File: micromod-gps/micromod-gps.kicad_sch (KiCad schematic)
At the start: 62 parts, among them J1 21992304, J2 Conn_01x08_Socket, Q1 2N7002, Q2 DMP510DL-7, SW1 KMR2, SW2 KMR2, U1 STM32G431CBTx, U10 TLV75533PDBV, U4 LMR51430, Y1 ECS-250-10-47Q-CES-TR

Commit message: tweaks
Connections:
- net MCU_UART_TX2: now reaches U1.10 (PA2)
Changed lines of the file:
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@@
-	)
-	(no_connect
-		(at 207.645 63.5)
 	)
 	(no_connect
@@
 	)
 	(no_connect
+		(at 229.235 63.5)
+	)
+	(no_connect
 		(at 318.135 65.405)
 	)
@@
 	(wire
 		(pts
+			(xy 207.645 63.5) (xy 229.235 63.5)
+		)
+		(stroke
+			(width 0)
+			(type default)
+		)
+	)
+	(wire
+		(pts
 			(xy 243.84 126.365) (xy 254.635 126.365)
 		)
@@
 		)
 	)
+	(label "MCU_UART_TX2"
+		(at 213.36 63.5 0)
+		(effects
+			(font
+				(size 1.27 1.27)
+			)
+			(justify left bottom)
+		)
+	)

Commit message: Added temp sensor and tvs diode for rs232
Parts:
- added C60: 0.1uF, Capacitor_SMD:C_0603_1608Metric_Pad1.08x0.95mm_HandSolder, symbol Device:C
- added U21: MCP9800Ax-xOT, Package_TO_SOT_SMD:SOT-23-5, symbol Sensor_Temperature:MCP9800Ax-xOT
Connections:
- net +3V3: now also C60.1, U21.1 (V_{DD})
- net GND: now also C60.2, U21.2 (GND)
- net GPS_SCL: now also U21.4 (SCLK)
- net GPS_SDA: now also U21.5 (SDA)
- net TOO_HOT: now reaches U1.28 (PB14)
- net TOO_HOT: now also U21.3 (ALERT)
- no-connect marks 48 -> 47

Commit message: Added testpoints
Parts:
- added TP10, TP11, TP2, TP3, TP4, TP5, TP8, TP9: TestPoint, SUFST:Keystone 5015, symbol Connector:TestPoint
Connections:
- net +3V3: now also TP10.1
- net +5V: now also TP9.1
- net +GLV_PROT: now also TP8.1
- net GPS_PPS: now also TP11.1
- net GPS_SCL: now also TP5.1
- net GPS_SDA: now also TP4.1
- net OFFBOARD_UART_IN: now also TP3.1
- net OFFBOARD_UART_OUT: now also TP2.1

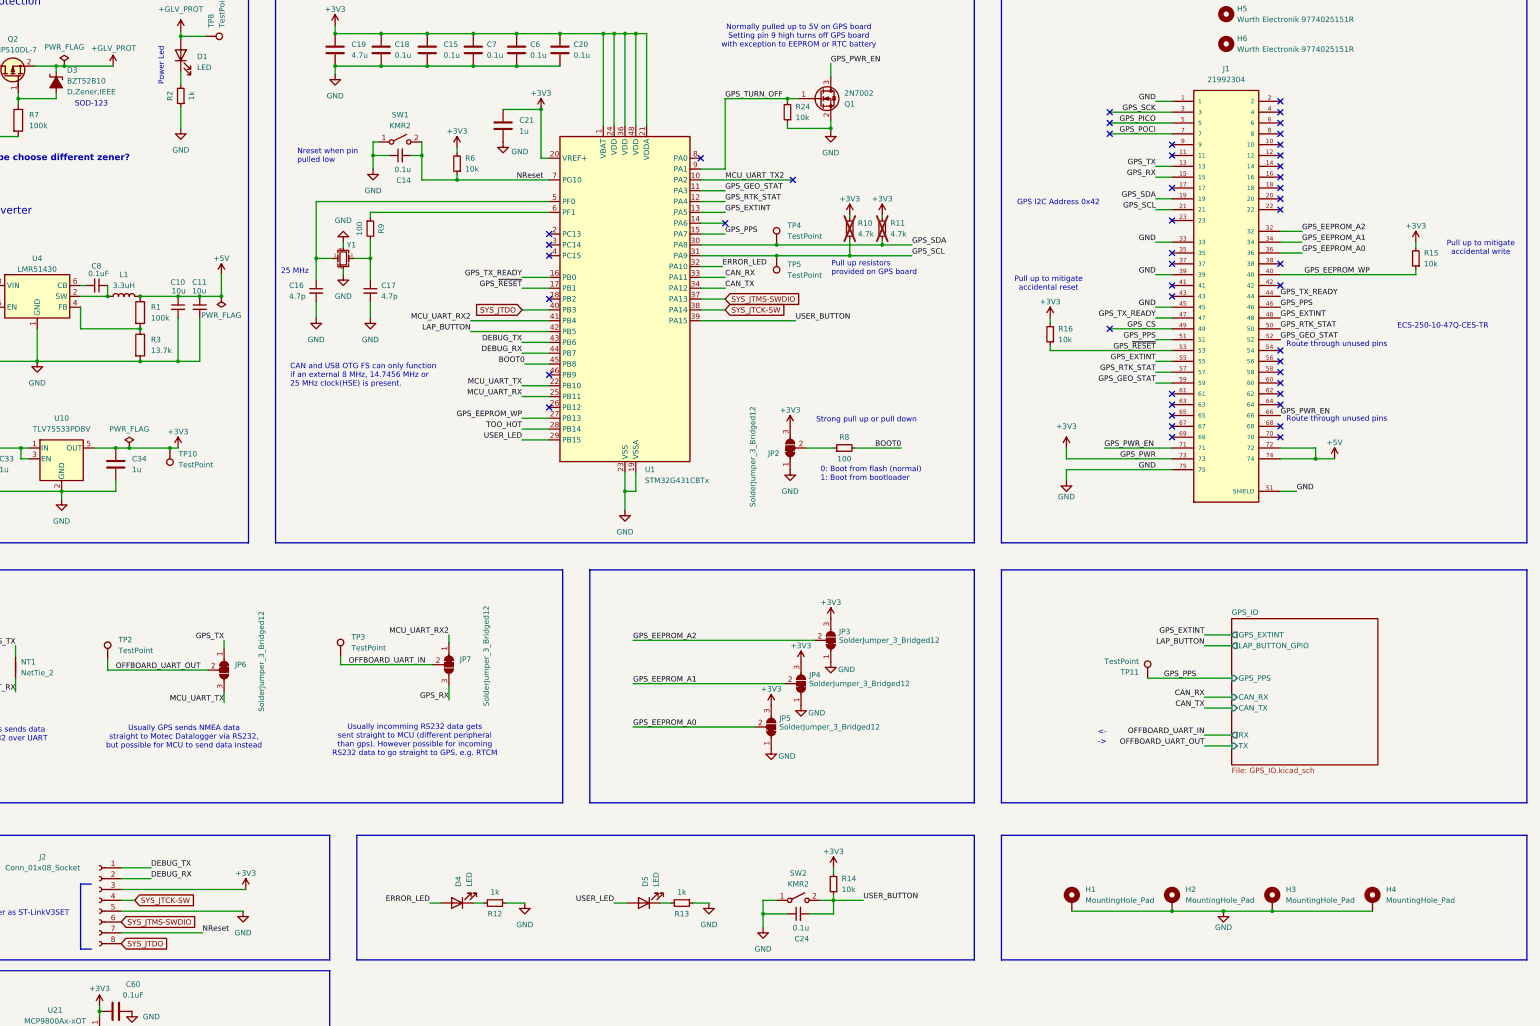
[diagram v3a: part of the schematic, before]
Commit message: rerouted some things and added SPI
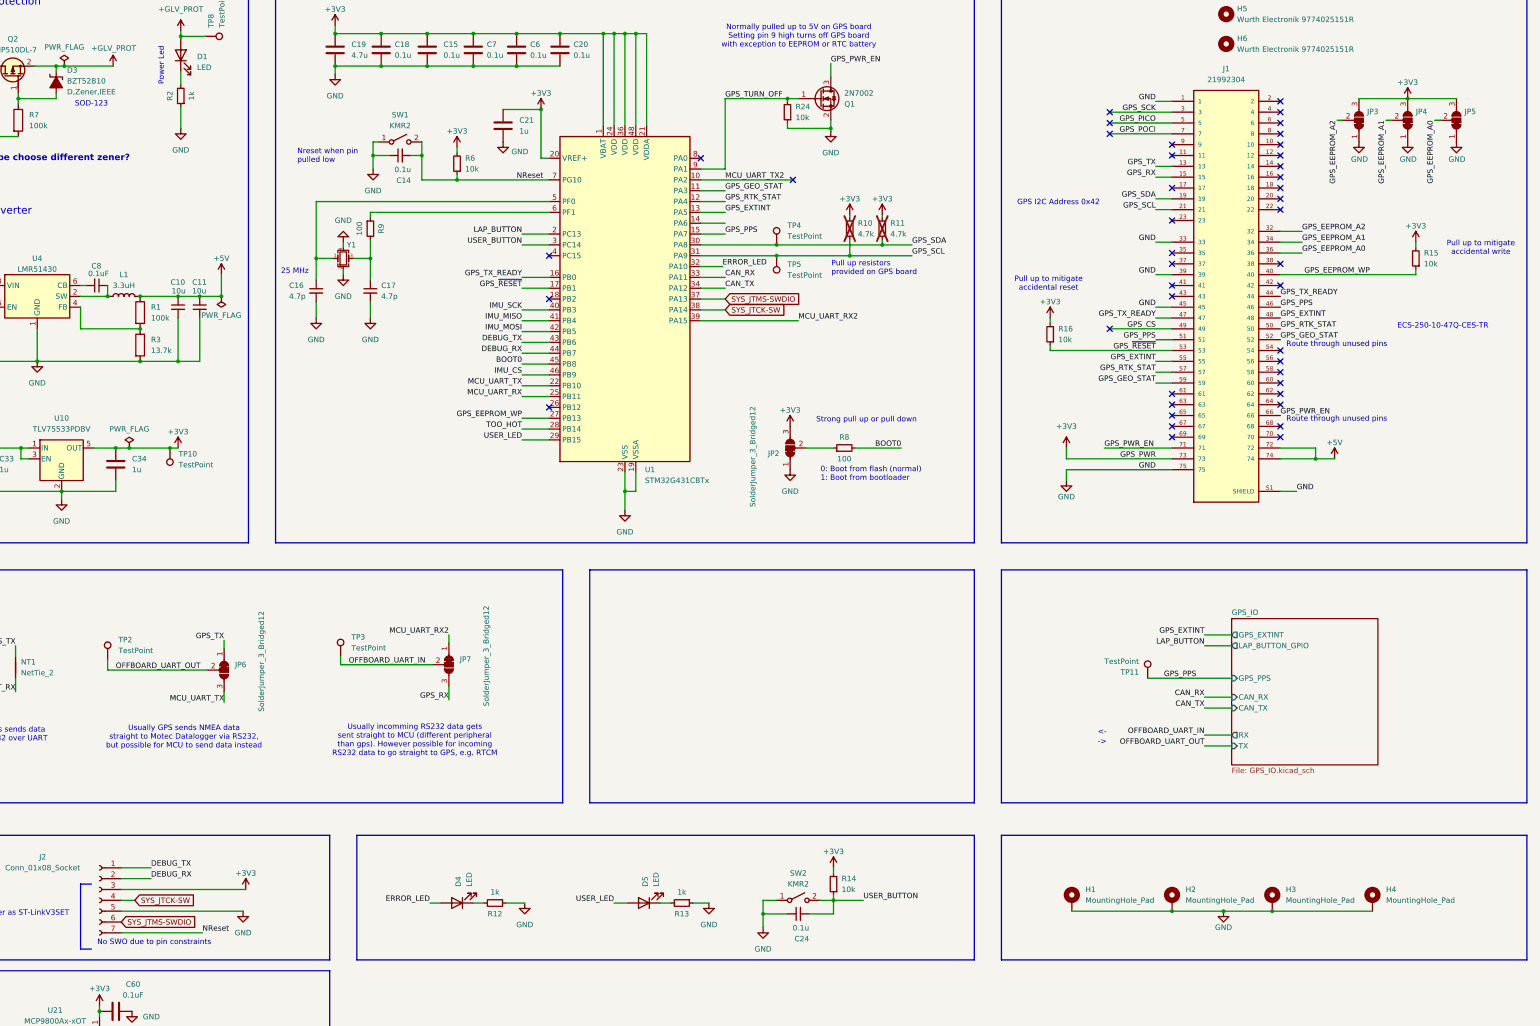
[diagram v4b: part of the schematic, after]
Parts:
- J2: footprint Connector_PinSocket_2.54mm:PinSocket_1x08_P2.54mm_Vertical -> Connector_PinSocket_2.54mm:PinSocket_1x07_P2.54mm_Vertical; symbol Connector:Conn_01x08_Socket -> Connector:Conn_01x07_Socket
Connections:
- net LAP_BUTTON: now also U1.2 (PC13); no longer U1.42 (PB5)
- net MCU_UART_RX2: now also U1.39 (PA15); no longer U1.41 (PB4)
- net USER_BUTTON: now also U1.3 (PC14); no longer U1.39 (PA15)
- net IMU_CS: now reaches U1.46 (PB9)
- net SYS_JTDO renamed IMU_SCK
- net IMU_SCK: no longer J2.8 (Pin_8)
- new net IMU_MISO: U1.41 (PB4)
- new net IMU_MOSI: U1.42 (PB5)
- no-connect marks 47 -> 43
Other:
- note added: "No SWO due to pin constraints"
- note removed: "CAN and USB OTG FS can only function if an external 8 MHz, 14.7456 MHz or 25 MHz clock(HSE) is present."
- moved on the sheet: JP3, JP4, JP5

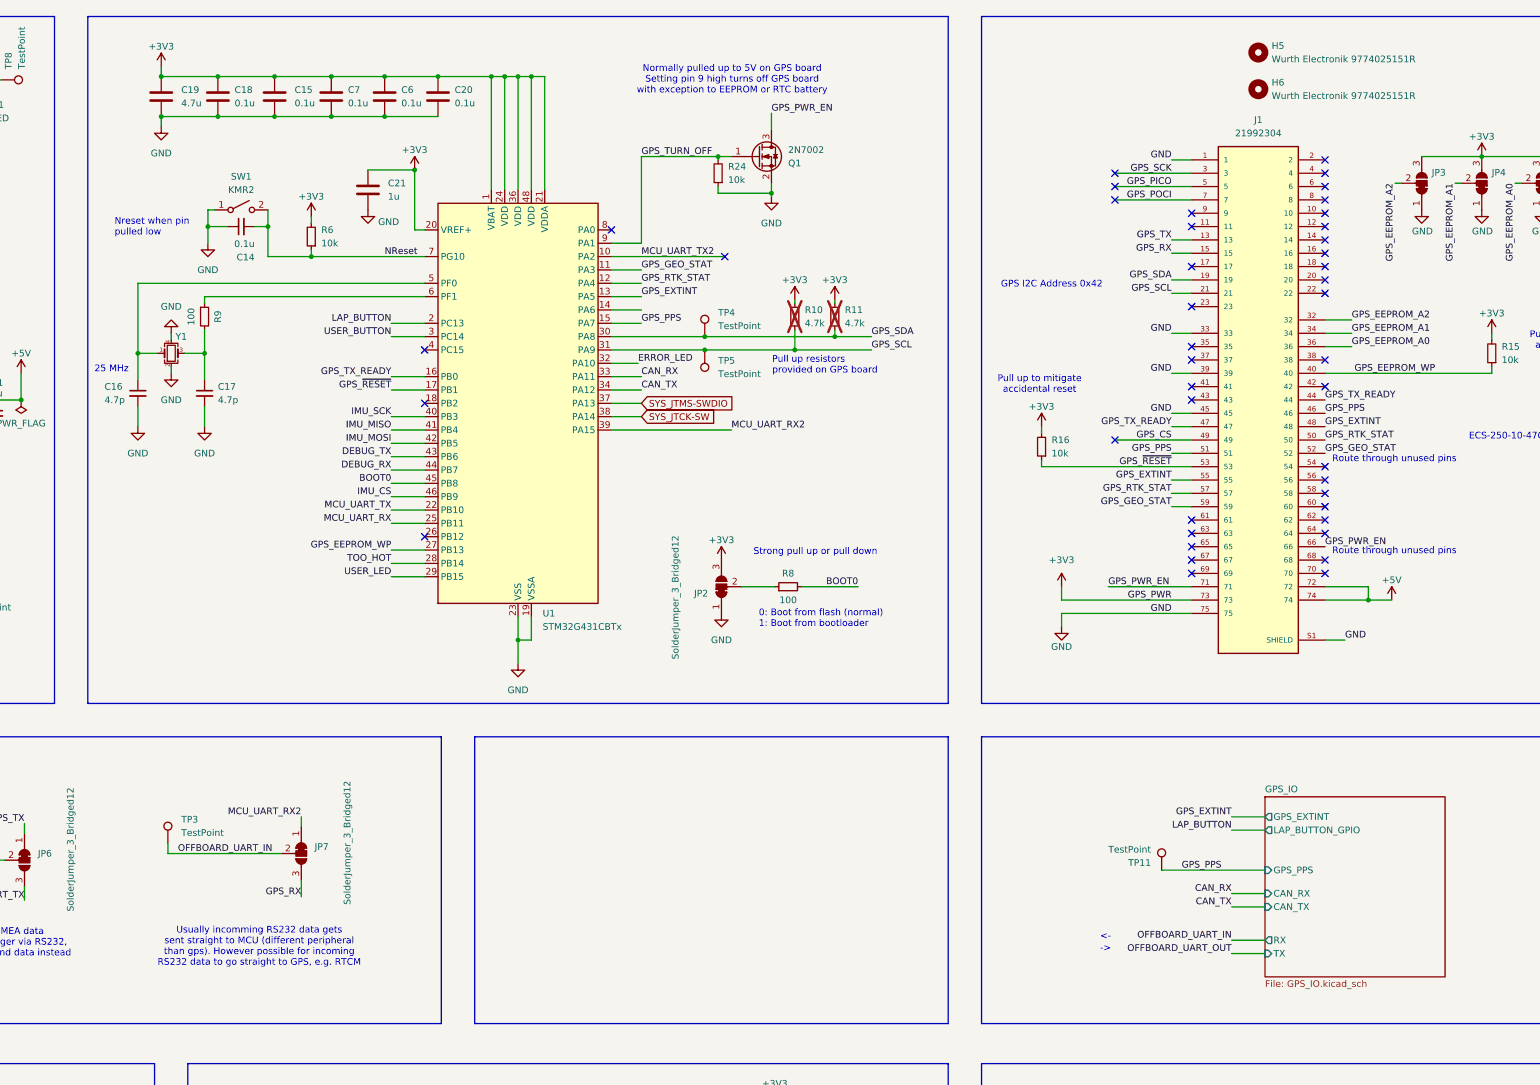
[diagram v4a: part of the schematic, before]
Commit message: Added IMU and Magnetometer
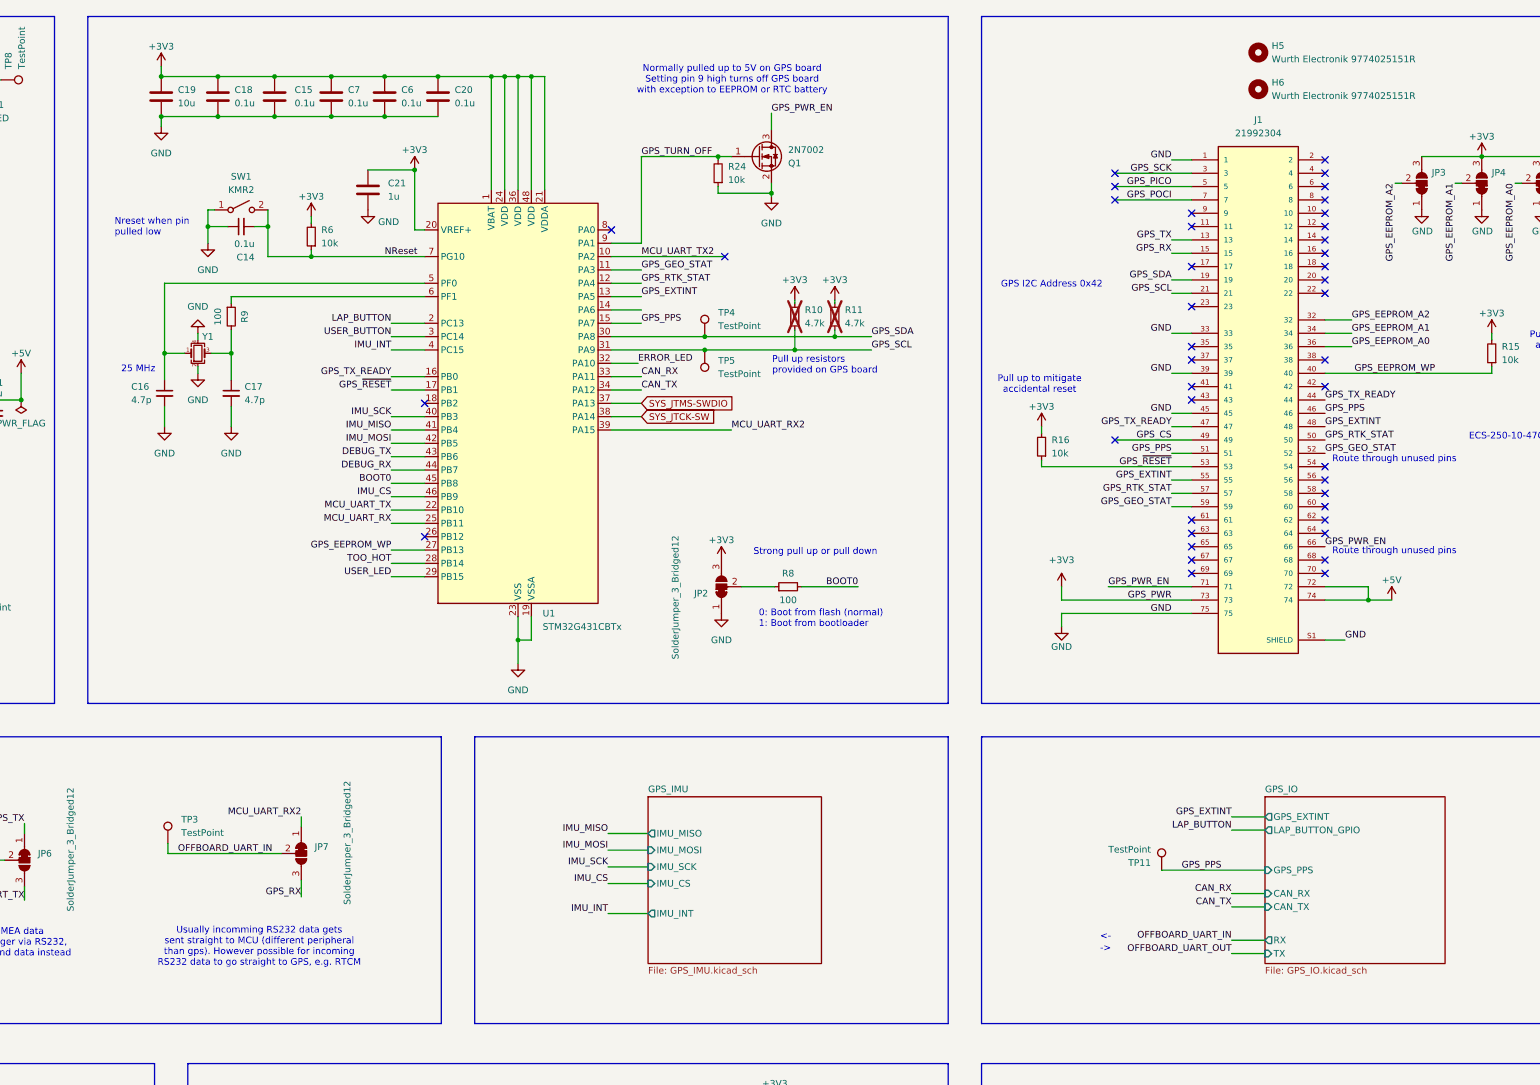
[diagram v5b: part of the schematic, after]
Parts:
- C19: value 4.7u -> 10u
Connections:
- net IMU_INT: now reaches U1.4 (PC15)
- no-connect marks 43 -> 42
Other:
- added sheet GPS_IMU (GPS_IMU.kicad_sch)
- moved on the sheet: C16, C17, R9, Y1

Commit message: adjust some things
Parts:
- R8: value 100 -> 10k
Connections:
- no-connect marks 42 -> 43
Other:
- note removed: "ECS-250-10-47Q-CES-TR"
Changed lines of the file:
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@@
 		)
 	)
-	(text "ECS-250-10-47Q-CES-TR"
-		(exclude_from_sim no)
-		(at 381.635 97.79 0)
-		(effects
-			(font
-				(size 1.27 1.27)
-			)
-		)
-	)
 	(text "Nreset when pin \npulled low"
 		(exclude_from_sim no)
@@
 	)
 	(no_connect
+		(at 207.645 73.66)
+	)
+	(no_connect
 		(at 229.235 63.5)
 	)
@@
 	(wire
 		(pts
-			(xy 207.645 73.66) (xy 213.36 73.66)
-		)
-		(stroke
-			(width 0)
-			(type default)
-		)
-	)
-	(wire
-		(pts
 			(xy 46.99 172.72) (xy 46.99 175.26)
 		)
@@
 		(on_board yes)
 		(dnp no)
-		(fields_autoplaced yes)
 		(property "Reference" "L1"
 			(at 72.39 85.725 90)
@@
 		)
 		(property "MPN" "XGL5020-322"
-			(at 72.39 90.805 90)
+			(at 72.39 79.502 90)
 			(effects
 				(font
 					(size 1.27 1.27)
 				)
-				(hide yes)
 			)
 		)
@@
 			)
 		)
-		(property "Value" "100"
+		(property "Value" "10k"
 			(at 241.3 128.905 90)
 			(effects
@@
 		)
 		(property "MPN" "ECS-250-10-47Q-CES-TR"
-			(at 128.905 81.915 0)
+			(at 129.032 104.902 0)
 			(effects
 				(font
 					(size 1.27 1.27)
 				)
-				(hide yes)
 			)
 		)

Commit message: Added some vias for grounding
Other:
- note added: "DO NOT REMOVE"
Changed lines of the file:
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@@
+		)
+	)
+	(text "DO NOT \nREMOVE"
+		(exclude_from_sim no)
+		(at 88.138 71.374 0)
+		(effects
+			(font
+				(size 3.81 3.81)
+				(thickness 0.762)
+				(bold yes)
+				(color 255 0 0 1)
+			)
 		)
 	)
@@
 		)
 		(stroke
+			(width 0)
+			(type default)
+		)
+	)
+	(wire
+		(pts
+			(xy 86.36 77.47) (xy 86.36 83.82)
+		)
+		(stroke

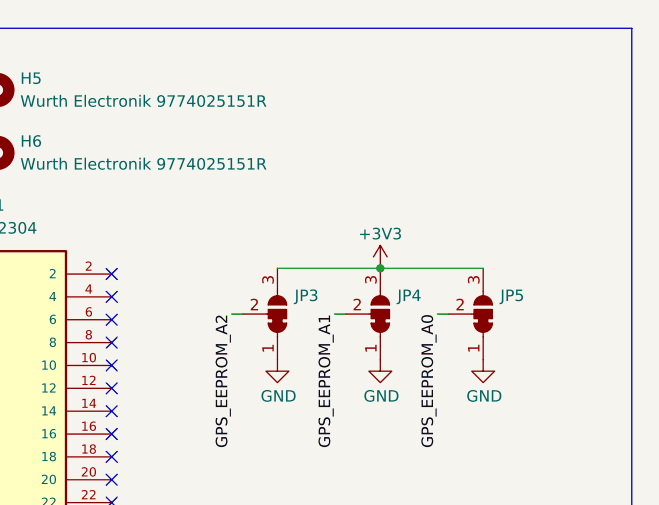
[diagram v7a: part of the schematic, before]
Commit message: Added pps tvs
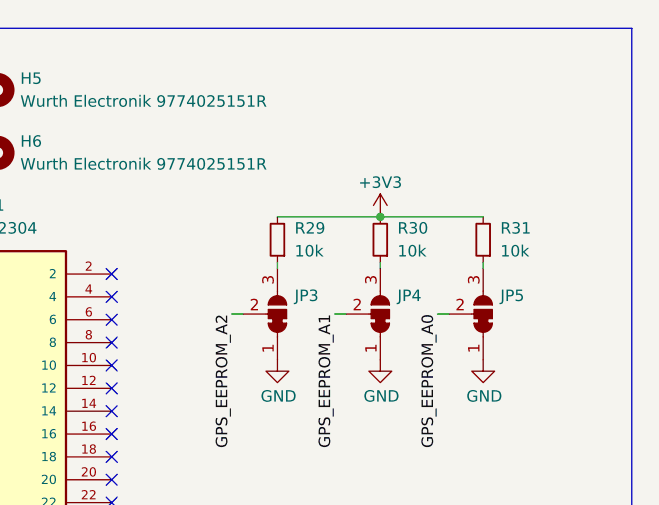
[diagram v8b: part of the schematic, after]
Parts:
- added R29, R30, R31: 10k, Resistor_SMD:R_0603_1608Metric_Pad0.98x0.95mm_HandSolder, symbol Device:R_Small
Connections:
- net +3V3: now also R29.2, R30.2, R31.2; no longer JP3.3 (B), JP4.3 (B), JP5.3 (B)
- new net: JP5.3 (B), R31.1
- new net: JP3.3 (B), R29.1
- new net: JP4.3 (B), R30.1
